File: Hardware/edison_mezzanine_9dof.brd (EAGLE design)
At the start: 30.5 x 44.5 mm, 31 parts, among them U1 LSM9DS0

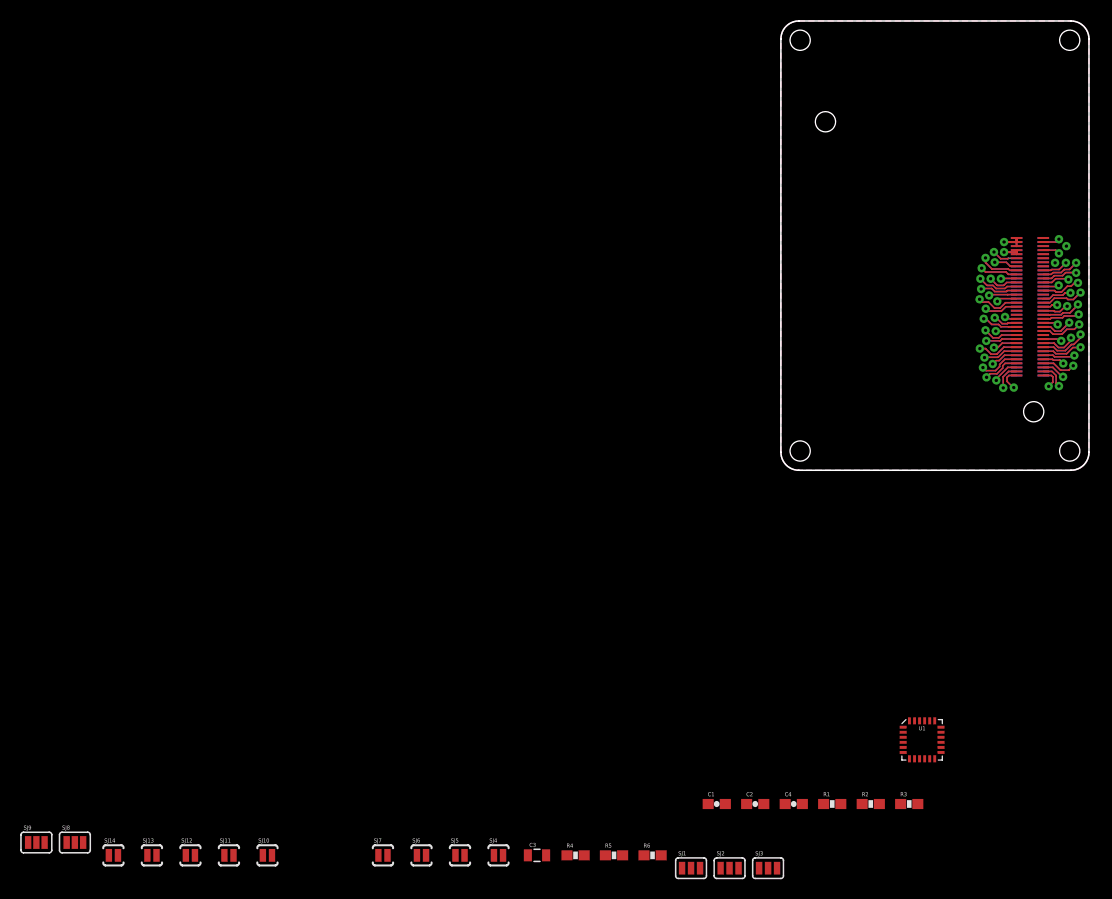
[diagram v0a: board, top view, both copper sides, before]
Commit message: Updated to new template. Initial component placement.
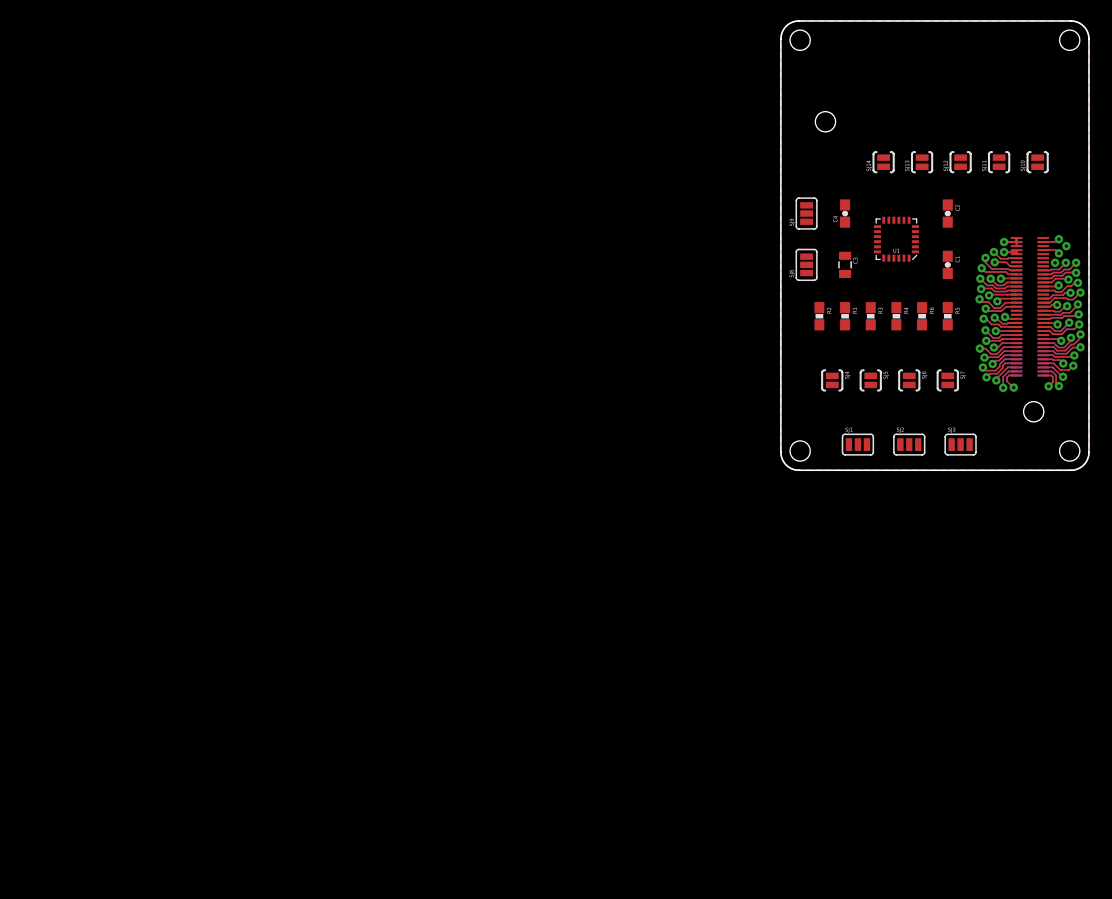
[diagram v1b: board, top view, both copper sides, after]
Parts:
- moved SJ10 102.5 mm to (25.4, 30.5), turned to 90 degrees
- moved SJ11 102.5 mm to (21.6, 30.5), turned to 90 degrees
- moved SJ12 102.5 mm to (17.8, 30.5), turned to 90 degrees
- moved SJ13 102.5 mm to (14.0, 30.5), turned to 90 degrees
- moved SJ14 102.5 mm to (10.2, 30.5), turned to 90 degrees
- moved SJ9 98.4 mm to (2.54, 25.4), turned to 90 degrees
- moved SJ8 92.2 mm to (2.54, 20.3), turned to 90 degrees
- moved SJ7 73.0 mm to (16.5, 8.89), turned to 270 degrees
- moved SJ6 67.4 mm to (12.7, 8.89), turned to 270 degrees
- moved C3 65.9 mm to (6.35, 20.3), turned to 270 degrees
- moved R5 62.7 mm to (16.5, 15.2), turned to 270 degrees
- moved SJ5 62.1 mm to (8.89, 8.89), turned to 270 degrees
- moved R4 62.1 mm to (11.4, 15.2), turned to 270 degrees
- moved C2 61.4 mm to (16.5, 25.4), turned to 270 degrees
- moved R6 59.6 mm to (14.0, 15.2), turned to 270 degrees
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- renumbered U$2 to U2, U$3 to U3
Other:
- board text added: "Edzzanine 9DOF"
- board text removed: "Example Name of Board"

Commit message: v01 board layout complete
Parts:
- removed FRAME2: FRAME-LETTER, SparkFun-Aesthetics:CREATIVE_COMMONS
- added LOGO1: SFE_LOGO_FLAME.3_INCH, SparkFun-Aesthetics:SFE_LOGO_FLAME_.3
- added SJ15: JUMPER-PAD-3-NOYES_SILK, SparkFun-Passives:PAD-JUMPER-3-NO_YES_SILK
- SJ1, SJ2, SJ3: value (none) -> JUMPER-PAD-3-NC_BY_PASTE; device SparkFun-Passives:SJ_3 -> SparkFun-Passives:PAD-JUMPER-3-NC_BY_PASTE_YES_SILK_FULL_BOX
- moved FRAME1 9.92 mm to (-8.89, -20.3)
- moved SJ12 5.24 mm to (12.7, 29.2)
- moved SJ13 5.24 mm to (8.89, 29.2)
- moved SJ14 5.24 mm to (5.08, 29.2)
- moved SJ10 5.24 mm to (20.3, 29.2)
- moved SJ11 5.24 mm to (16.5, 29.2)
- moved C3 5.08 mm to (6.35, 25.4), turned to 90 degrees
- moved C4 5.08 mm to (6.35, 20.3), turned to 270 degrees
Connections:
- net GND: now also SJ15.2
- net SDO_G: now also SJ15.3
- net SDO_XM: now also SJ15.1
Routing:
- net GP47: track 5.51 -> 72.5 mm, vias 1 -> 3
- net GP48: track 4.04 -> 63.8 mm, vias 1 -> 3
- net VSYS: track 4.48 -> 63.0 mm, vias 1 -> 5
- net GP109_SPI_2_CLK: track 9.36 -> 62.1 mm, vias 1 -> 2
- net GP115_SPI_2_TXD: track 8.10 -> 57.0 mm, vias 1 -> 2
- net GP20_I2C_1_SDA: track 2.97 -> 49.7 mm, vias 1 -> 2
- net GP19_I2C_1_SCL: track 7.37 -> 49.4 mm, vias 1 -> 2
- net SDO_G: track 0.00 -> 40.2 mm, vias 0 -> 2
- net GP46: track 7.39 -> 41.8 mm, vias 1 -> 2
- net GP110_SPI_2_FS0: track 6.97 -> 37.4 mm, vias 1 -> 2
- net GP44: track 5.93 -> 36.0 mm, vias 1 -> 3
- net SDO_XM: track 0.00 -> 28.9 mm
- net SCL: track 0.00 -> 27.0 mm, vias 0 -> 2
- net GP49: track 8.47 -> 34.8 mm, vias 1 -> 2
- net GP111_SPI_2_FS1: track 3.70 -> 28.7 mm, vias 1 -> 2
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- added copper zone on layer 1, net VSYS
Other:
- board text added: "CLOCK"
- board text added: "CS Pullups"
- board text added: "CSG"
- board text added: "CSXM"
- board text added: "DATA"
- board text added: "DEN"
- board text added: "DRDYG"
- board text added: "I2C Addr GND"
- board text added: "I2C Addr Pullups"
- board text added: "I2C Pullups"
- board text added: "INT1"
- board text added: "INT2"
- board text added: "INTG"
- board text added: "MOSI"
- board text added: "SCK"
- board text added: "SCL"
- board text added: "SDA"
- board text added: "SDOG"
- board text added: "Shawn Hymel"
- board text added: "v01"
- board text removed: "Casey Kuhns"

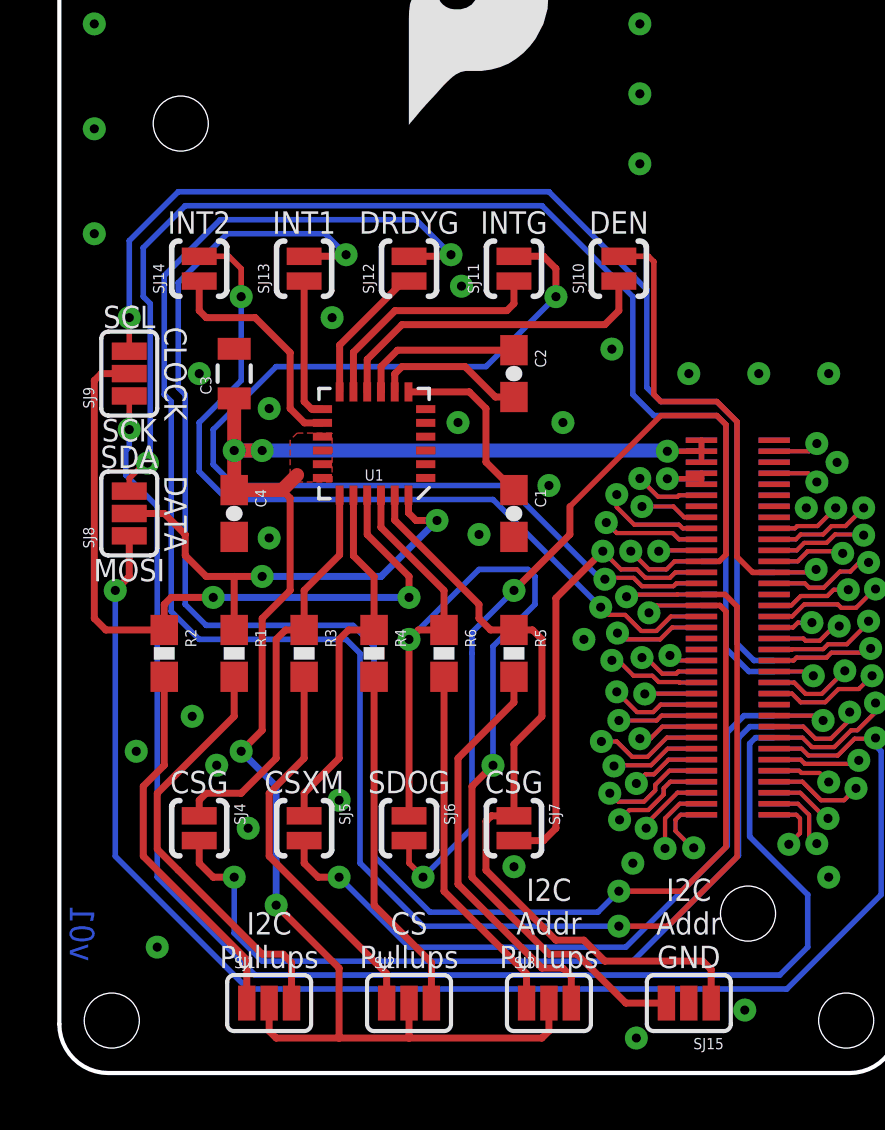
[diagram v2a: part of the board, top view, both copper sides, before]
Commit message: Added LDO
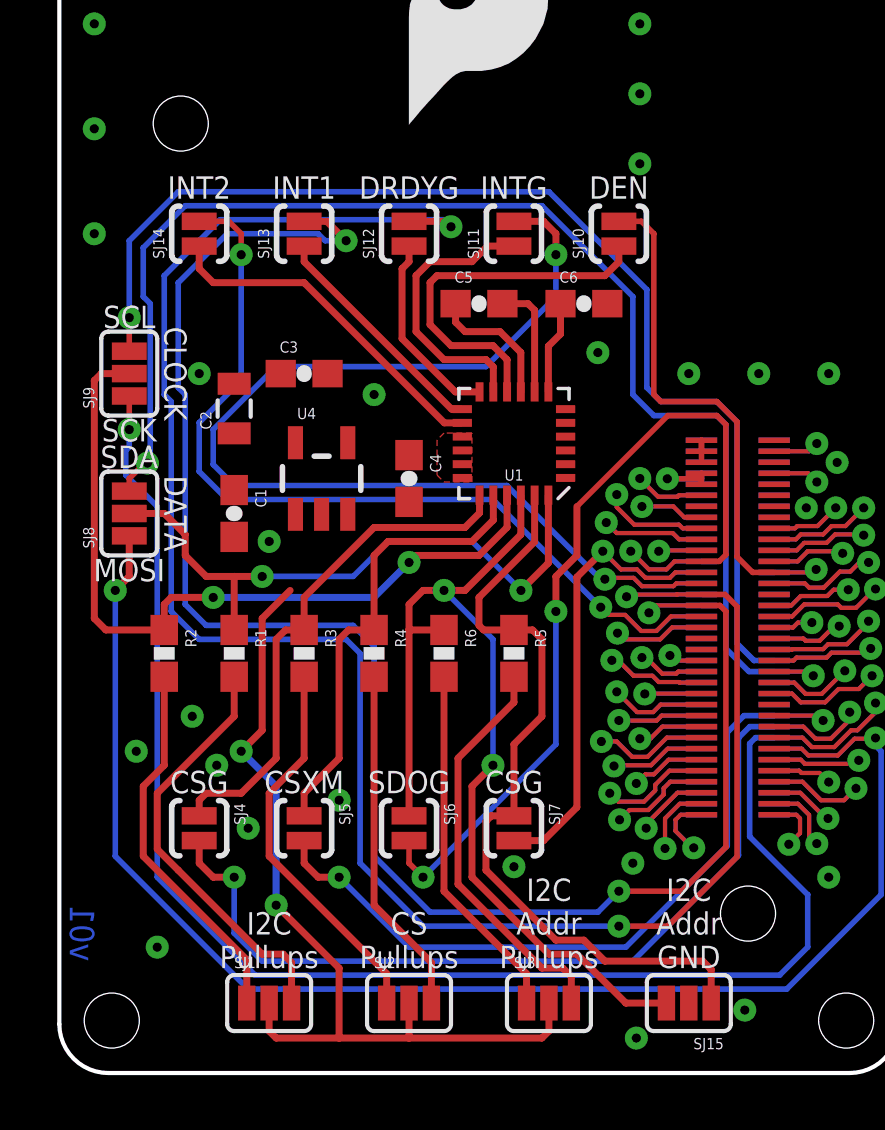
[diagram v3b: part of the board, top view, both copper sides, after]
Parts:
- added C5: 0.22uF, SparkFun-Capacitors:0603-CAP
- added C6: 4.7uF, SparkFun-Capacitors:0603-CAP
- added U4: (no value), SparkFun-PowerIC:SOT23-5
- C1: value 4.7uF -> 1.0uF
- C2: value 0.22uF -> 10uF; device SparkFun-Capacitors:0603-CAP -> SparkFun-Capacitors:0805
- C3: value 10uF -> 1.0uF; device SparkFun-Capacitors:0805 -> SparkFun-Capacitors:0603-CAP
- C4: value 1.0uF -> 0.1uF
- moved C2 10.2 mm to (6.35, 24.1), turned to 90 degrees
- moved C1 10.2 mm to (6.35, 20.3)
- moved C4 6.48 mm to (12.7, 21.6)
- moved U1 5.08 mm to (16.5, 22.9)
- moved C3 2.54 mm to (8.89, 25.4), turned to 0 degrees
- moved SJ10 1.27 mm to (20.3, 30.5)
- moved SJ11 1.27 mm to (16.5, 30.5)
- moved SJ12 1.27 mm to (12.7, 30.5)
- moved SJ13 1.27 mm to (8.89, 30.5)
- moved SJ14 1.27 mm to (5.08, 30.5)
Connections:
- new net 3.3V_LOCAL: C2.1, C3.1, C4.1, SJ1.2, SJ2.2, SJ3.2, U1.15, U1.16, U1.17, U1.18, U4.5
- net GND: now also C2.2, C6.2, U4.2
- net N$1: now also C5.1; no longer C2.1
- net N$2: now also C5.2; no longer C2.2
- net N$3: now also C6.1; no longer C1.1
- net VSYS: now also C1.1, U4.1, U4.3; no longer C3.1, C4.1, SJ1.2, SJ2.2, SJ3.2, U1.15, U1.16, U1.17, U1.18
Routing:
- net VSYS: track 63.0 -> 1.20 mm, vias 5 -> 0
- net 3.3V_LOCAL: track 0.00 -> 32.1 mm, vias 0 -> 2
- net SDA: track 17.1 -> 22.7 mm
- net SDO_G: track 40.2 -> 35.9 mm
- net INT2_XM: track 8.43 -> 12.7 mm
- net CS_G: track 14.9 -> 18.9 mm
- net INT1_XM: track 5.15 -> 8.53 mm
- net CS_XM: track 13.6 -> 16.8 mm
- net N$3: track 6.45 -> 3.39 mm
- net DRDY_G: track 5.18 -> 7.08 mm
- net DEN_G: track 12.1 -> 13.8 mm
- net INT_G: track 8.82 -> 10.3 mm
- net SCL: track 27.0 -> 28.4 mm
- net N$2: track 5.55 -> 4.23 mm
- net GP46: track 41.8 -> 43.1 mm
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- added copper zone on layer 1, net 3.3V_LOCAL
- removed copper zone on layer 1, net VSYS

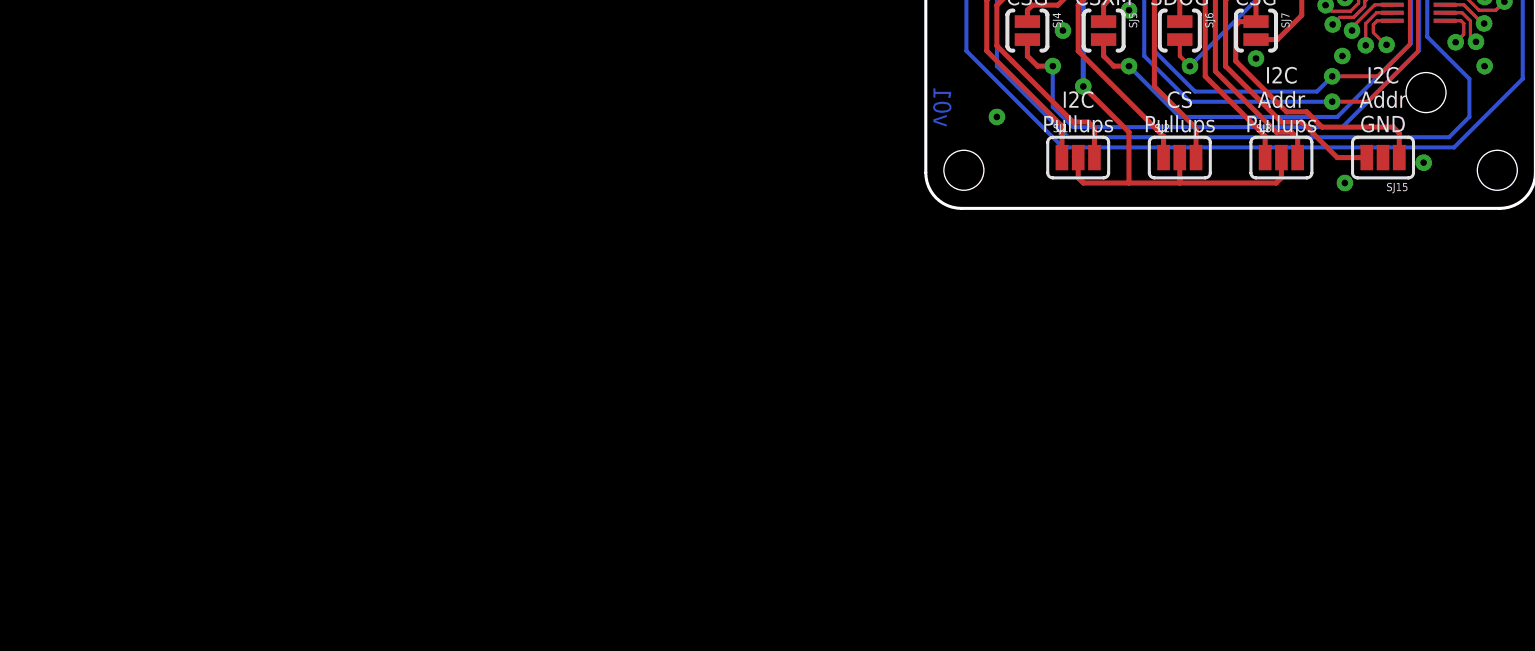
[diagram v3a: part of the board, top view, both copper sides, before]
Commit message: Changed to 1.8V IO and added 4x 2-way jumpers for address select.
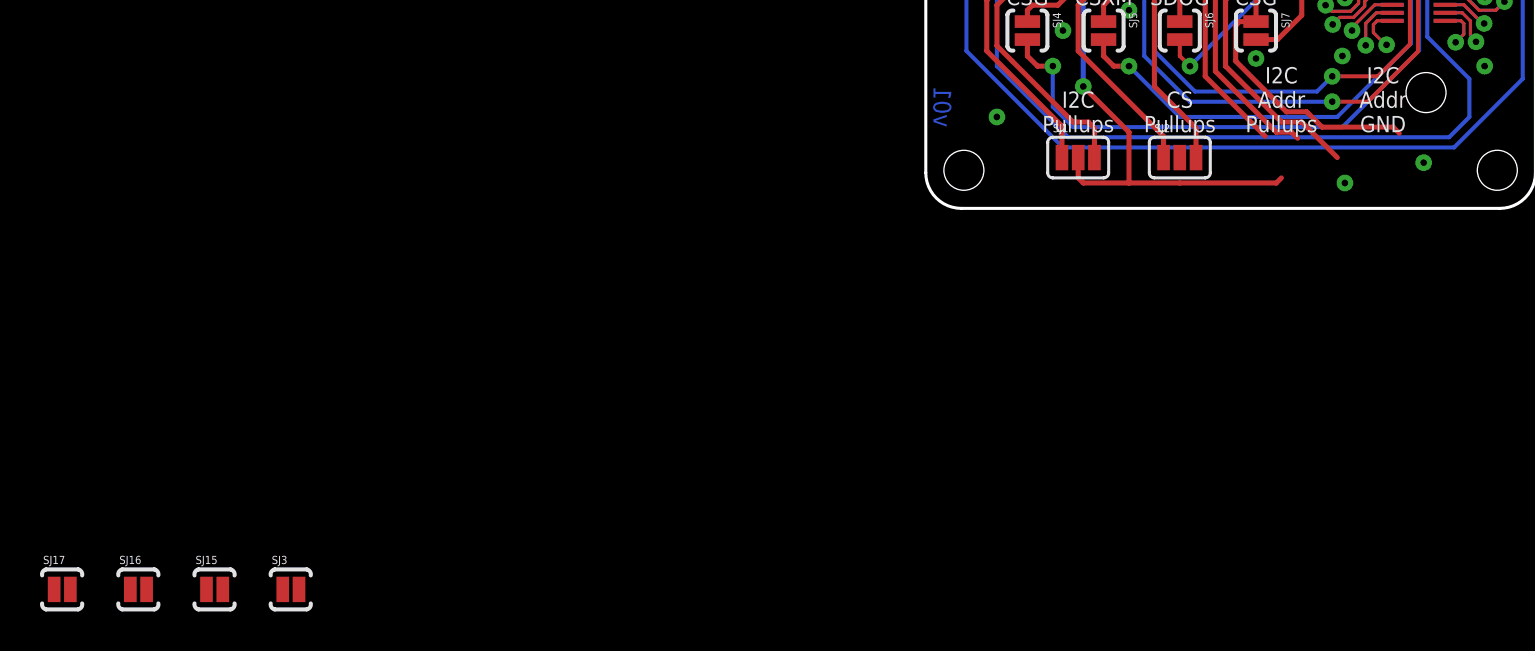
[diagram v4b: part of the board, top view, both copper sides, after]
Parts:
- added SJ16, SJ17: JUMPER-PAD-2-NC_BY_PASTE, SparkFun-Passives:PAD-JUMPER-2-NC_BY_PASTE_YES_SILK
- SJ15: value JUMPER-PAD-3-NOYES_SILK -> JUMPER-PAD-2-NC_BY_PASTE; device SparkFun-Passives:PAD-JUMPER-3-NO_YES_SILK -> SparkFun-Passives:PAD-JUMPER-2-NC_BY_PASTE_YES_SILK
- SJ3: value JUMPER-PAD-3-NC_BY_PASTE -> JUMPER-PAD-2-NC_BY_PASTE; device SparkFun-Passives:PAD-JUMPER-3-NC_BY_PASTE_YES_SILK_FULL_BOX -> SparkFun-Passives:PAD-JUMPER-2-NC_BY_PASTE_YES_SILK
- moved SJ15 62.3 mm to (-35.6, -19.1), turned to 0 degrees
- moved SJ3 54.0 mm to (-31.8, -19.1)
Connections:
- net 1.8V: now also SJ1.2, SJ15.2, SJ2.2, SJ3.2, U1.18
- net 3.3V_LOCAL: no longer SJ1.2, SJ2.2, SJ3.2, U1.18
- net GND: now also SJ16.1, SJ17.1; no longer SJ15.2
- net N$12: now also SJ3.1; no longer SJ3.3
- net N$13: now also SJ15.1; no longer SJ3.1
- net SDO_G: now also SJ17.2; no longer SJ15.3
- net SDO_XM: now also SJ16.2; no longer SJ15.1
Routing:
- net 3.3V_LOCAL: track 32.1 -> 0.00 mm, vias 2 -> 0
- net 1.8V: track 5.06 -> 34.9 mm, vias 1 -> 3
- net SDO_G: track 35.9 -> 34.4 mm
- net SDO_XM: track 28.7 -> 27.4 mm
- net N$13: track 13.1 -> 12.0 mm
- net N$12: track 14.8 -> 13.9 mm
